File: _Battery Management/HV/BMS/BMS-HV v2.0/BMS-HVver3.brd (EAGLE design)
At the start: 152.4 x 124.8 mm, 422 parts, among them J3 M2S02B-PASK-2(LF)(SN), J4 M2S02B-PASK-2(LF)(SN), Q1 BSS308PE, Q10 BSS308PE, Q11 BSS308PE, Q12 BSS308PE, Q13 BSS308PE, Q14 BSS308PE, Q15 BSS308PE, Q16 BSS308PE, Q17 BSS308PE, Q18 BSS308PE, Q19 BSS308PE, Q2 BSS308PE, Q20 BSS308PE, Q21 BSS308PE, Q22 BSS308PE, Q23 BSS308PE, Q24 BSS308PE, Q25 BSS308PE, Q26 BSS308PE, Q27 BSS308PE, Q28 BSS308PE, Q29 BSS308PE, Q3 BSS308PE, Q30 BSS308PE, Q31 BSS308PE, Q32 BSS308PE, Q33 BSS308PE, Q34 BSS308PE, Q35 BSS308PE, Q36 BSS308PE, Q37 BSS308PE, Q38 BSS308PE, Q39 BSS308PE, Q4 BSS308PE, Q5 BSS308PE, Q6 BSS308PE, Q7 BSS308PE, Q8 BSS308PE, Q9 BSS308PE, U1 LTC6804-2, U2 LTC6804-2, U3 LTC6804-2

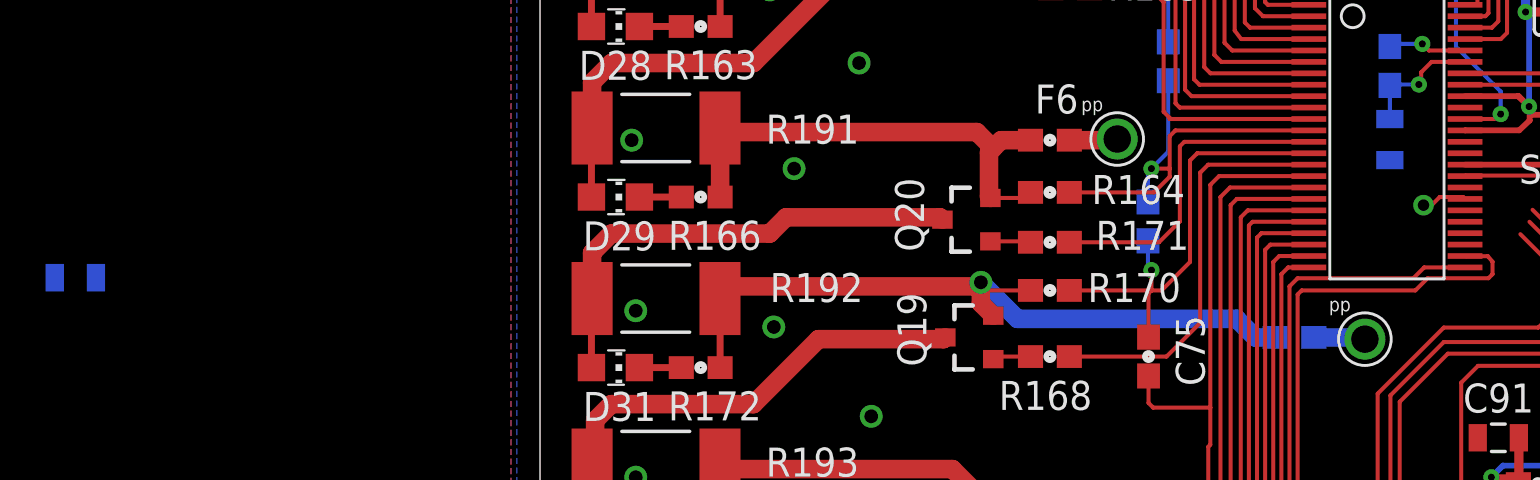
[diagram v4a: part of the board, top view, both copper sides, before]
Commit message: 
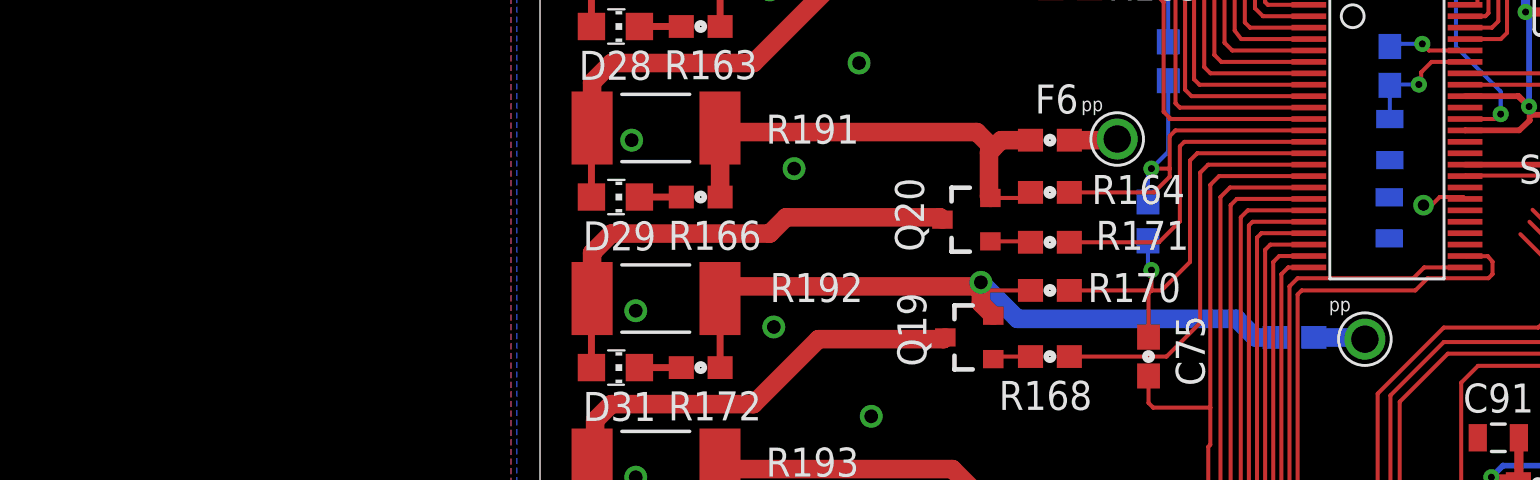
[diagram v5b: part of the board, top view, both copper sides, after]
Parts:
- moved C90 57.6 mm to (-39.0, 5.31), turned to 270 degrees
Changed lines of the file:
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@@
 <attribute name="VALUE" x="-44.9326" y="-51.1556" size="0.4064" layer="27" font="vector" rot="R270"/>
 </element>
-<element name="C90" library="FSAE Electric" package="0805" value="1UF" x="-96.5454" y="2.6924" smashed="yes" rot="MR0">
-<attribute name="PARTNO" value="UMK212F105ZG-T" x="436.6006" y="-1030.0716" size="1.778" layer="28" rot="MR0" display="off"/>
-<attribute name="NAME" x="-98.3234" y="2.2479" size="1.27" layer="26" font="vector" ratio="20" rot="MR0"/>
-<attribute name="VALUE" x="-95.5294" y="1.2954" size="0.4064" layer="28" rot="MR0"/>
+<element name="C90" library="FSAE Electric" package="0805" value="1UF" x="-39.0144" y="5.3086" smashed="yes" rot="MR270">
+<attribute name="PARTNO" value="UMK212F105ZG-T" x="993.7496" y="538.4546" size="1.778" layer="28" rot="MR270" display="off"/>
+<attribute name="NAME" x="-36.9443" y="7.112" size="1.27" layer="26" font="vector" ratio="20" rot="MR270"/>
+<attribute name="VALUE" x="-37.6174" y="6.3246" size="0.4064" layer="28" rot="MR270"/>
 </element>
 <element name="C91" library="FSAE Electric" package="0805" value="1UF" x="-34.2392" y="-4.318" smashed="yes" rot="R180">
@@
 <vertex x="-77.216" y="-59.69"/>
 </polygon>
-<wire x1="-72.009" y1="1.2446" x2="-97.4454" y2="2.6924" width="0" layer="19" extent="16-16"/>
 </signal>
 <signal name="IPA">
@@
 <contactref element="U3" pad="35"/>
 <contactref element="C90" pad="1"/>
-<wire x1="-35.695375" y1="8.14" x2="-95.6454" y2="2.6924" width="0" layer="19" extent="1-16"/>
+<wire x1="-35.695375" y1="8.14" x2="-39.0144" y2="6.2086" width="0" layer="19" extent="1-16"/>
 </signal>
 <signal name="N$135">

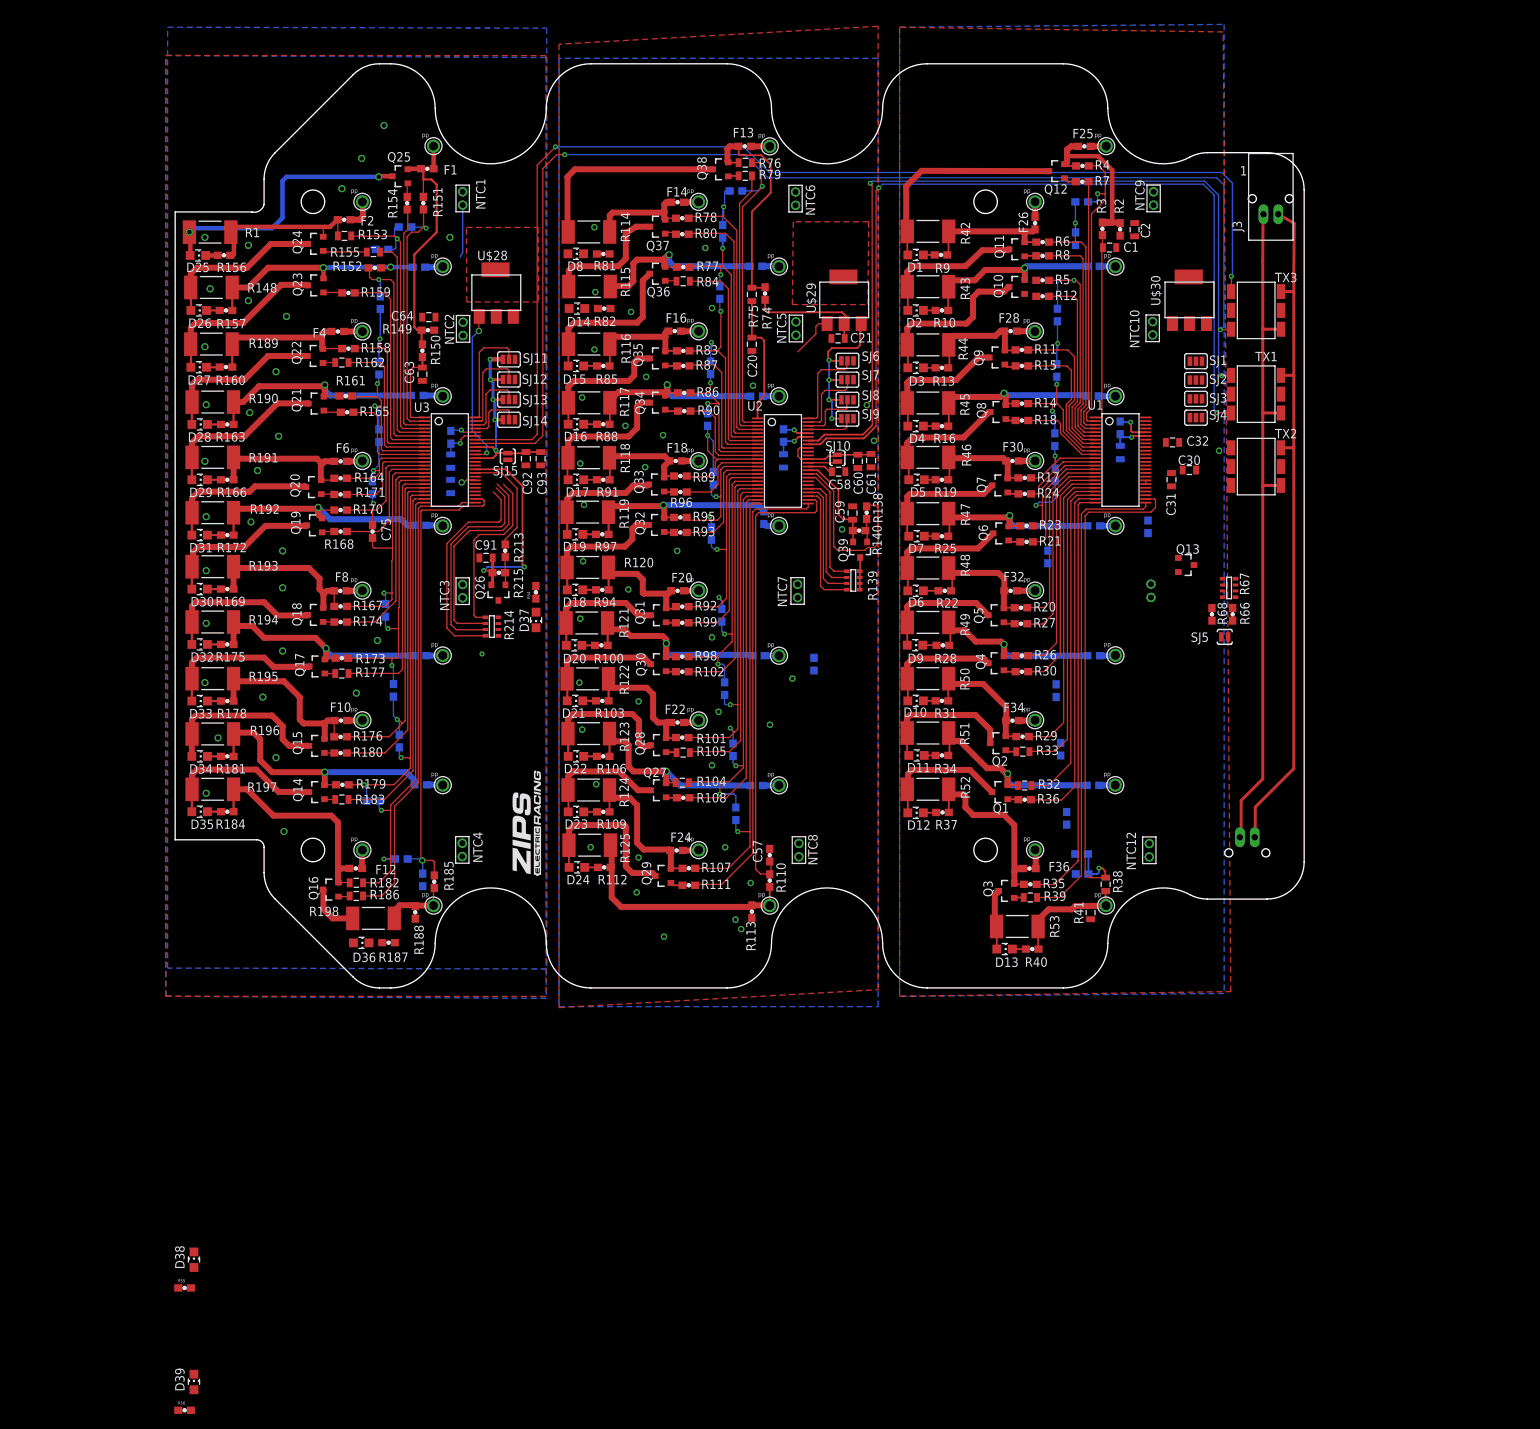
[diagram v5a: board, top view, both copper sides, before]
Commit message: 
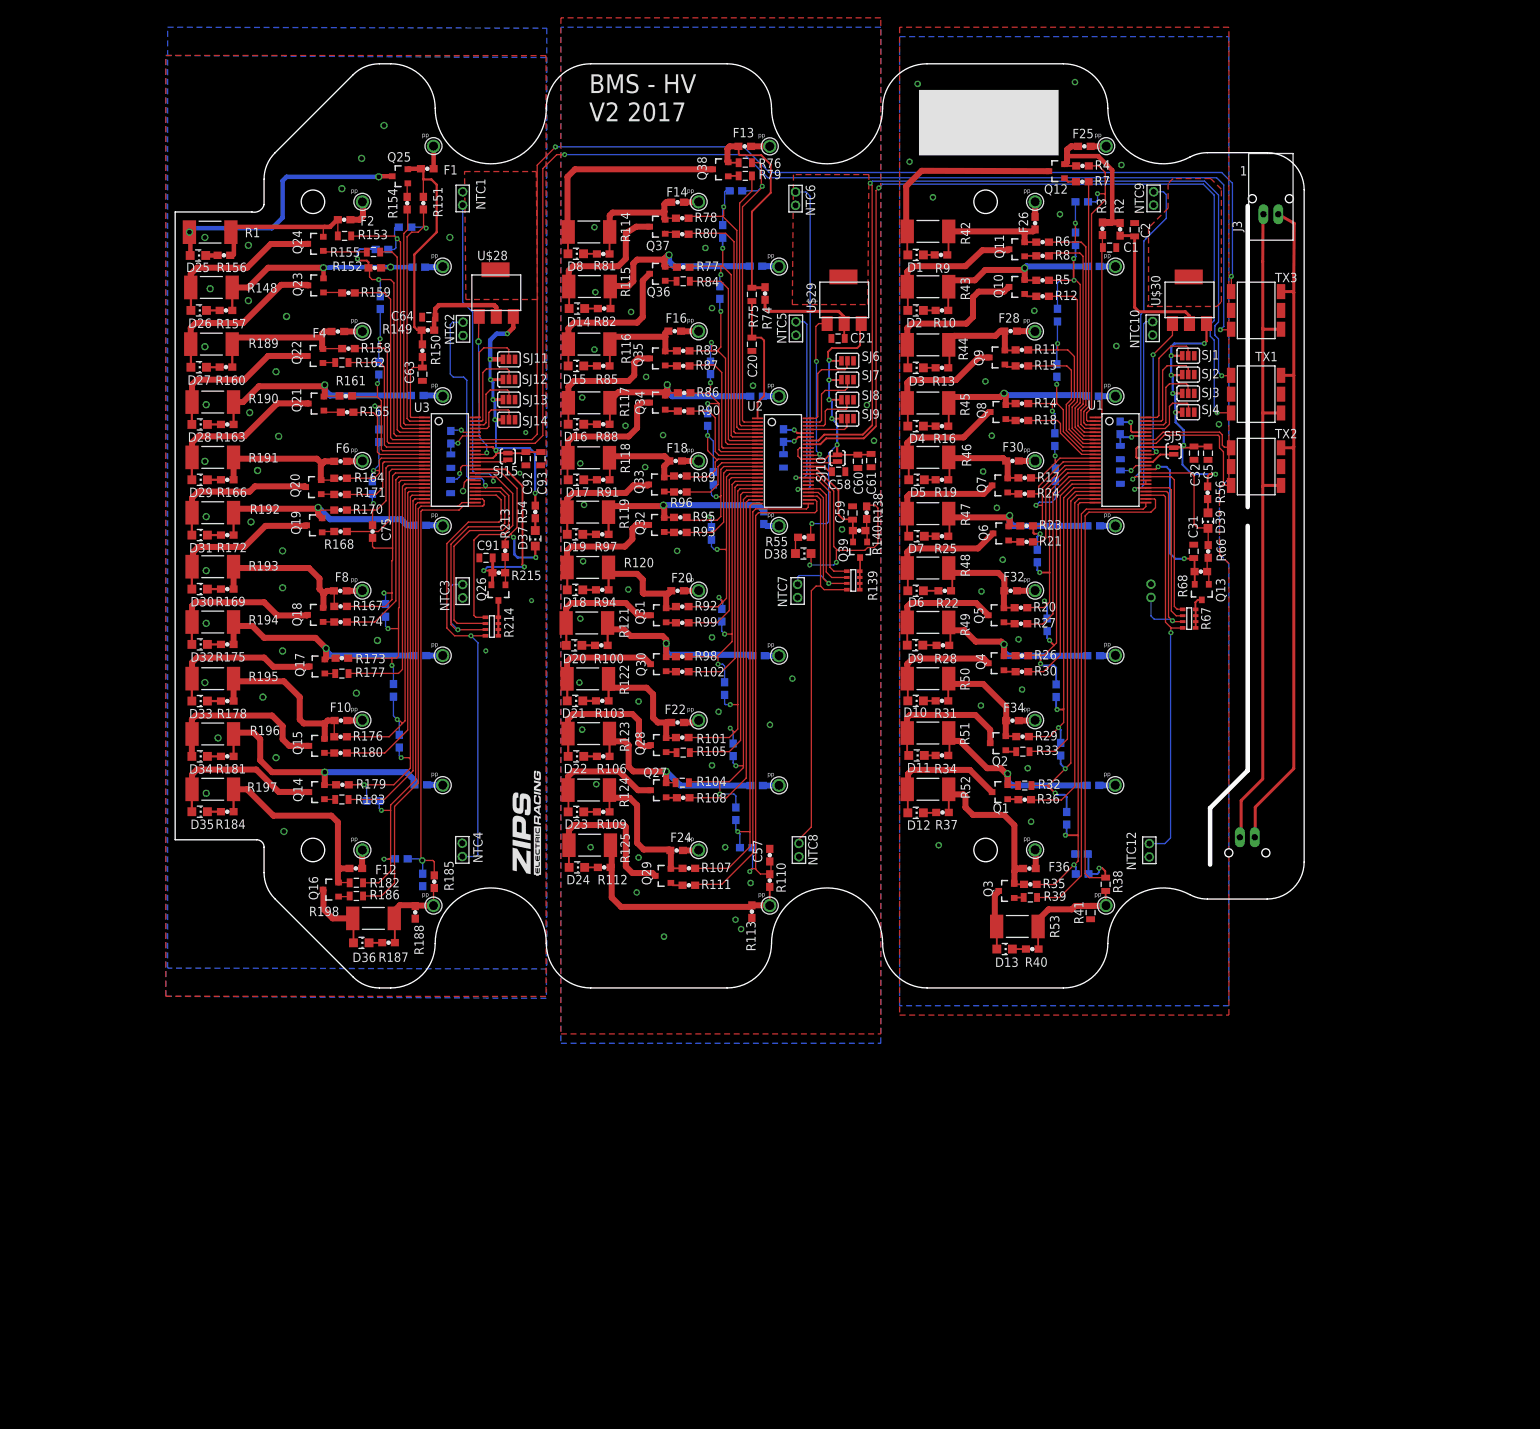
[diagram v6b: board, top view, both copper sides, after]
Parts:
- added C5: 1UF, FSAE Electric:0805
- moved R56 185.5 mm to (63.2, 4.47), turned to 90 degrees
- moved D39 179.6 mm to (63.2, 0.71), turned to 180 degrees
- moved R55 131.4 mm to (8.74, -1.55)
- moved D38 125.9 mm to (8.59, -3.73), turned to 270 degrees
- moved C55 26.4 mm to (0.89, -43.4), turned to 180 degrees
- moved SJ5 26.0 mm to (58.6, 10.1), turned to 90 degrees
- moved C17 19.0 mm to (41.5, -13.4)
- moved D37 11.0 mm to (-27.6, -1.68)
- moved R54 10.8 mm to (-27.6, 1.88)
- moved C31 10.1 mm to (61.3, -3.44), turned to 90 degrees
- moved C30 9.36 mm to (51.4, 6.58), flipped to the bottom, turned to 270 degrees
- moved R66 9.10 mm to (63.2, -3.45)
- moved R67 6.75 mm to (60.7, -12.5), turned to 270 degrees
- moved R68 5.96 mm to (62.3, -6.17), turned to 180 degrees
- moved Q13 4.20 mm to (62.4, -8.89), turned to 180 degrees
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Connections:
- net GNDI: now also C5.2
- net GPIO11: now also U3.29; no longer U3.28
- net GPIO12: now also U3.32; no longer U3.27
- net GPIO13: now also U3.27; no longer U3.32
- net GPIO14: now also U3.28; no longer U3.29
- net GPIO6: now also U1.29; no longer U1.28
- net GPIO7: now also U1.32; no longer U1.27
- net GPIO8: now also U1.27; no longer U1.32
- net GPIO9: now also U1.28; no longer U1.29
- net VREG1: now also C5.1
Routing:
- net GPIO7: track 0.00 -> 66.5 mm, vias 0 -> 1
- net GPIO8: track 0.00 -> 53.9 mm, vias 0 -> 1
- net VREG1: track 0.00 -> 51.3 mm, vias 0 -> 7
- net GPIO6: track 0.00 -> 47.9 mm, vias 0 -> 1
- net GPIO3: track 16.3 -> 60.9 mm, vias 0 -> 1
- net GPIO12: track 31.1 -> 68.9 mm, vias 0 -> 1
- net GPIO1: track 17.3 -> 53.6 mm
- net GPIO13: track 29.9 -> 64.3 mm, vias 0 -> 1
- net GPIO11: track 29.3 -> 59.7 mm, vias 0 -> 1
- net GPIO9: track 0.00 -> 27.7 mm, vias 0 -> 1
- net GPIO4: track 16.4 -> 41.6 mm, vias 0 -> 1
- net VREF4: track 0.00 -> 22.0 mm, vias 0 -> 2
- net VREG2: track 32.0 -> 52.7 mm, vias 5 -> 7
- net N$50: track 0.00 -> 20.5 mm
- net VREG: track 37.5 -> 57.8 mm, vias 4 -> 6
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- added copper zone on layer 1, net N$141
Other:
- outline, holes or cut-outs redrawn
- board text added: "BMS - HV"
- board text added: "V2 2017"
